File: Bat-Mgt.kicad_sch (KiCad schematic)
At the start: 0 parts

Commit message: Add power
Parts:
- added C34: 2u2, Capacitor_SMD:C_0402_1005Metric, symbol Device:C
- added C35, C37: 100n, Capacitor_SMD:C_0201_0603Metric, symbol Device:C_Small
- added C36: 1u, Capacitor_SMD:C_0402_1005Metric, symbol Device:C
- added U4: AP2112K-3.3, Package_TO_SOT_SMD:SOT-23-5, symbol Regulator_Linear:AP2112K-3.3
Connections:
- new net GND: C34.2, C35.2, C36.2, C37.2, U4.2 (GND)
- new net VDD_MCU: C36.1, C37.1, U4.5 (VOUT)
- new net VIN: C34.1, C35.1, U4.1 (VIN), U4.3 (EN)

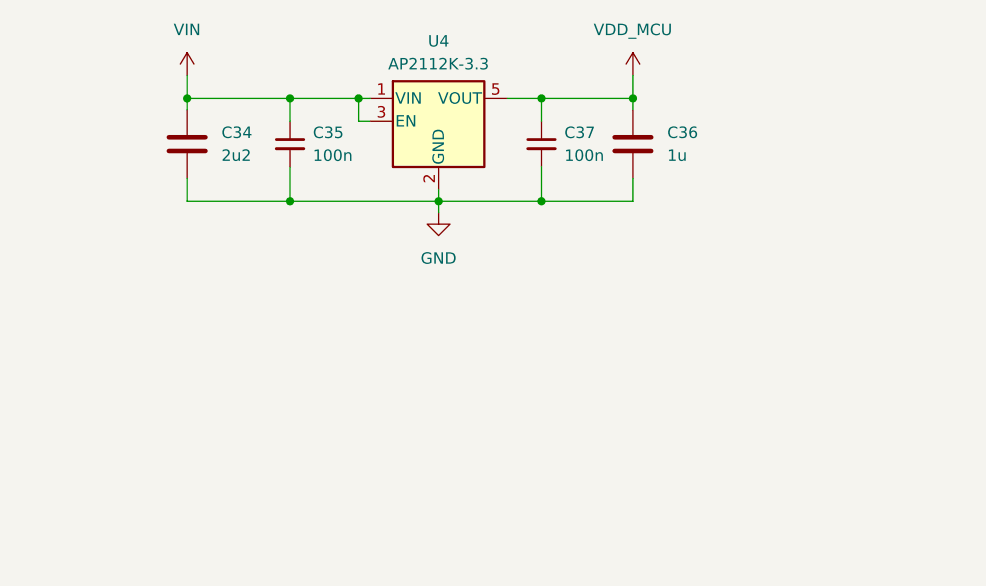
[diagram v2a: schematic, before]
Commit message: Changed PMIC to dc-dc converter, finished track
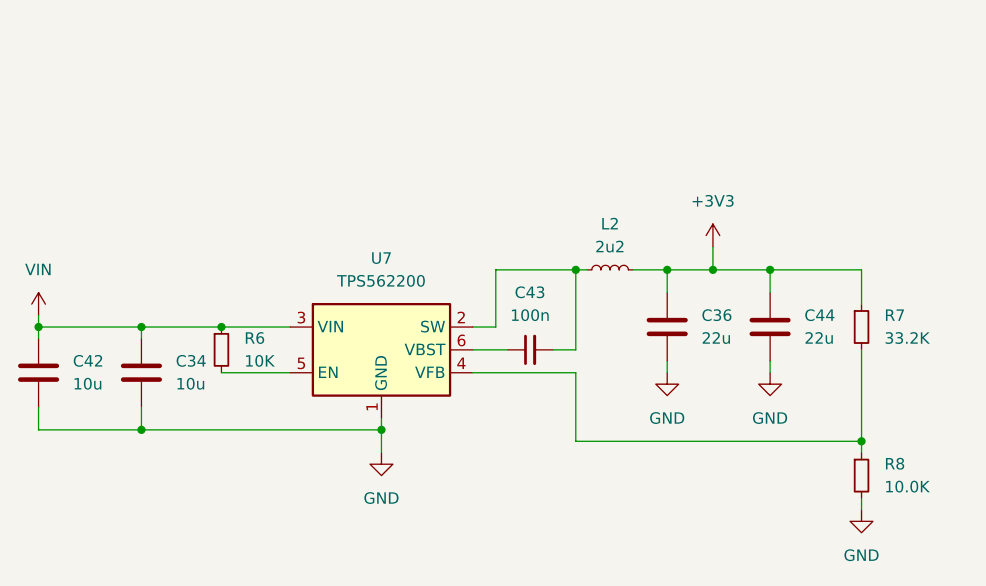
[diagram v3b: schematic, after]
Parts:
- removed C35, C37: 100n, Capacitor_SMD:C_0201_0603Metric, symbol Device:C_Small
- removed U4: AP2112K-3.3, Package_TO_SOT_SMD:SOT-23-5, symbol Regulator_Linear:AP2112K-3.3
- added C42: 10u, Capacitor_SMD:C_0603_1608Metric, symbol Device:C
- added C43: 100n, Capacitor_SMD:C_0402_1005Metric, symbol Device:C_Small
- added C44: 22u, Capacitor_SMD:C_0603_1608Metric, symbol Device:C
- added L2: 2u2, Inductor_SMD:L_0805_2012Metric, symbol Device:L_Small
- added R6: 10K, Resistor_SMD:R_0402_1005Metric, symbol Device:R_Small
- added R7: 33.2K, Resistor_SMD:R_0402_1005Metric, symbol Device:R_Small
- added R8: 10.0K, Resistor_SMD:R_0402_1005Metric, symbol Device:R_Small
- added U7: TPS562200, Package_TO_SOT_SMD:SOT-23-6, symbol Regulator_Switching:TPS562200
- C34: value 2u2 -> 10u; footprint Capacitor_SMD:C_0402_1005Metric -> Capacitor_SMD:C_0603_1608Metric
- C36: value 1u -> 22u; footprint Capacitor_SMD:C_0402_1005Metric -> Capacitor_SMD:C_0603_1608Metric
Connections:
- net GND: now also C42.2, C44.2, R8.2, U7.1 (GND)
- net VIN: now also C42.1, R6.1, U7.3 (VIN)
- net VDD_MCU renamed +3V3
- net +3V3: now also C44.1, L2.2, R7.1
- new net: C43.2, L2.1, U7.2 (SW)
- new net: R7.2, R8.1, U7.4 (VFB)
- new net: C43.1, U7.6 (VBST)
- new net: R6.2, U7.5 (EN)
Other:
- moved on the sheet: C34, C36

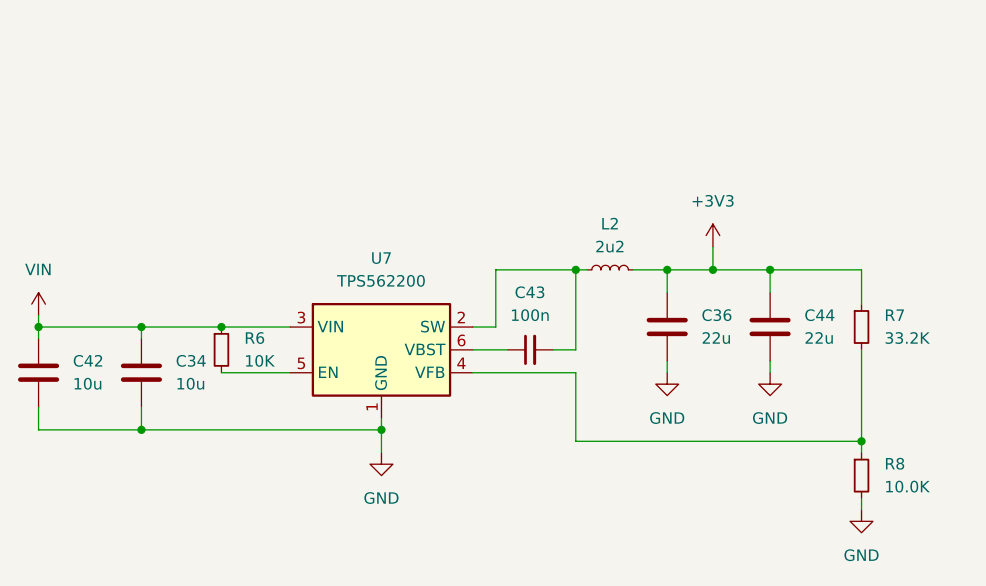
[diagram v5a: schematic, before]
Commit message: Adding JLCPCB Part #
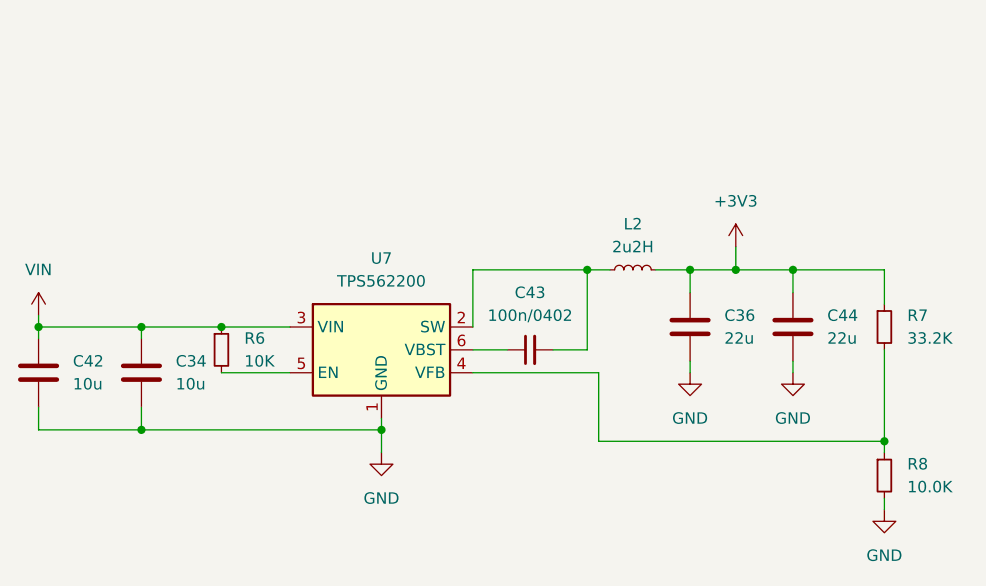
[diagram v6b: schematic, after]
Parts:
- C34, C42: JLCPCB Part # (none) -> C96446
- C36, C44: JLCPCB Part # (none) -> C59461
- C43: value 100n -> 100n/0402; JLCPCB Part # (none) -> C307331
- L2: value 2u2 -> 2u2H; JLCPCB Part # (none) -> C162585
- R6: footprint Resistor_SMD:R_0402_1005Metric -> Resistor_SMD:R_0201_0603Metric; JLCPCB Part # (none) -> C473048
- R7: JLCPCB Part # (none) -> C226998
- R8: JLCPCB Part # (none) -> C25804
- U7: JLCPCB Part # (none) -> C49757
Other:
- moved on the sheet: C36, C44, L2, R7, R8

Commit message: Optimize layout with lowest impedance as possible
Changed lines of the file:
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@@
 (kicad_sch
-	(version 20231120)
+	(version 20250114)
 	(generator "eeschema")
-	(generator_version "8.0")
+	(generator_version "9.0")
 	(paper "A4")
 	(junction
